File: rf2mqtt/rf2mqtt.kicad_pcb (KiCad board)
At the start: 2 copper layers, 64 x 56.5 mm, 25 parts, among them J1 Antenna Wire, Q1 TN0106N3-G, SW1 config, U1 Pico

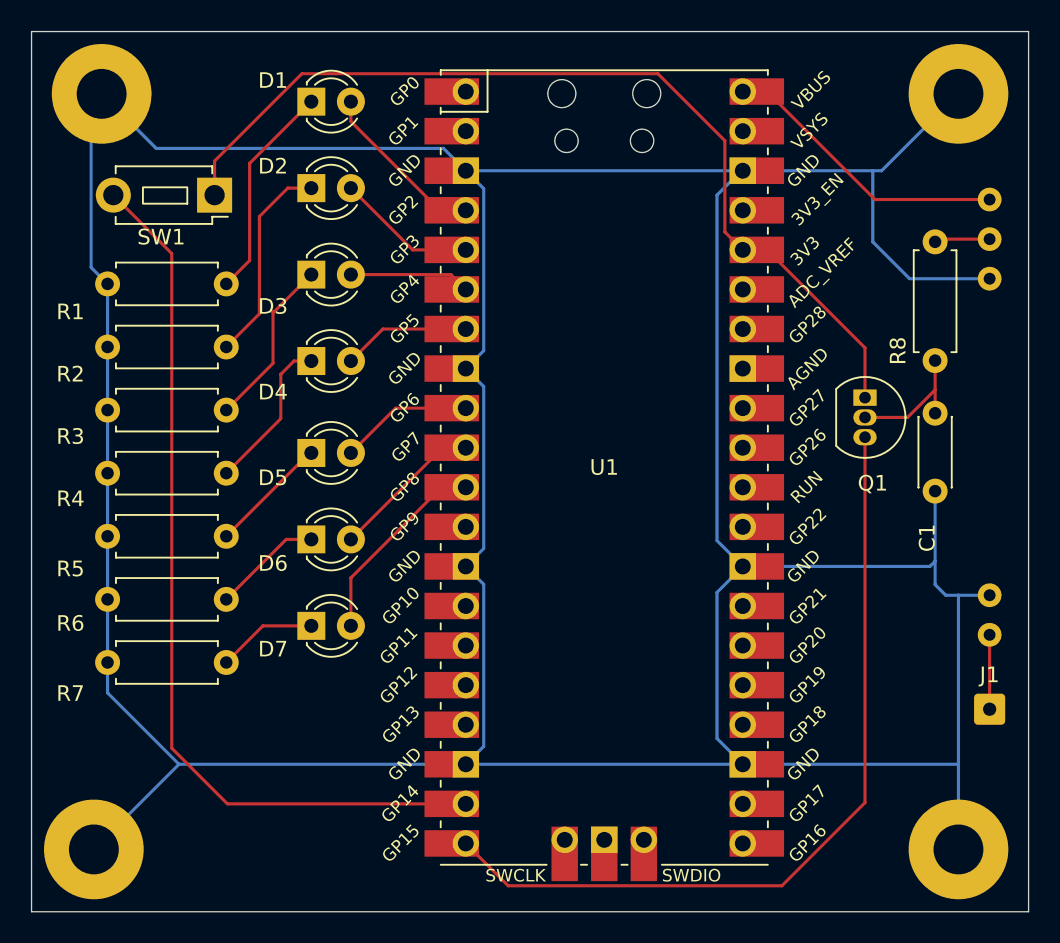
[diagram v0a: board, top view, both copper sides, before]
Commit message: Add debug MQTT messages
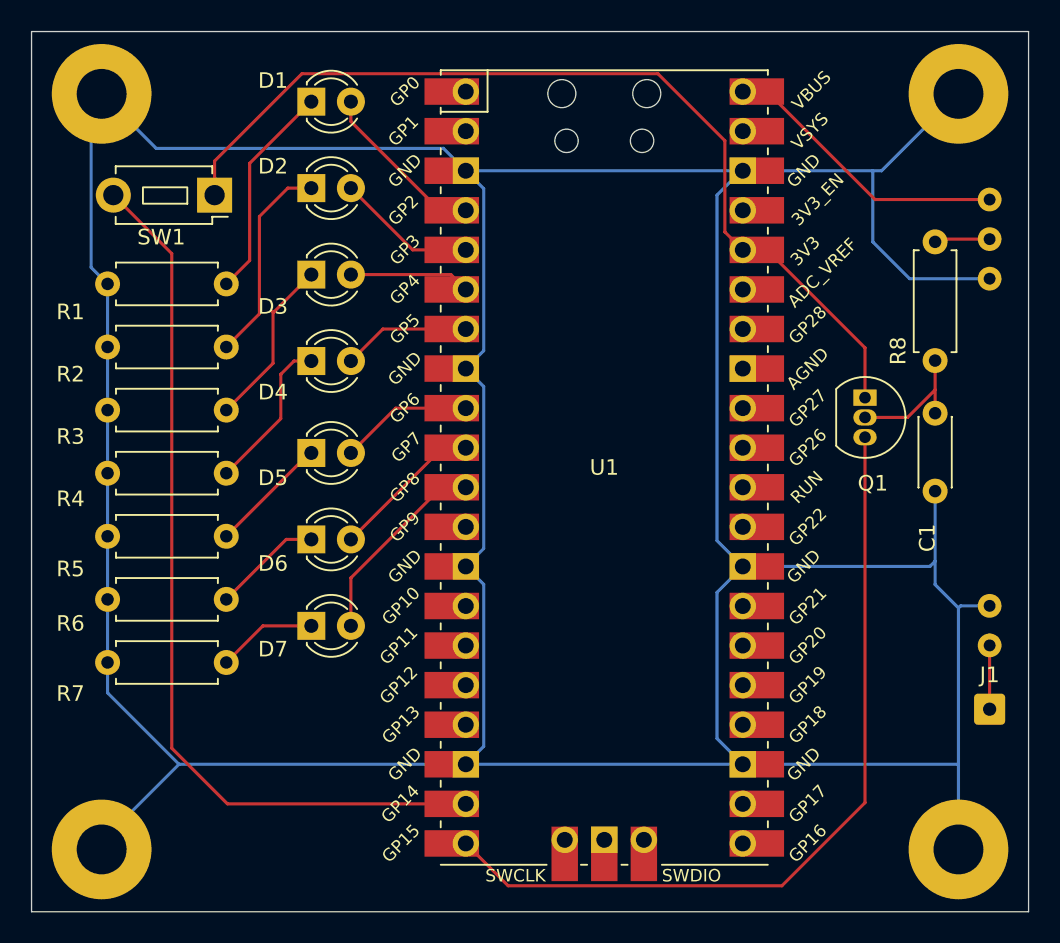
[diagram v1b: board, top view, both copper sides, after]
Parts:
- moved REF1 0.50 mm to (103.0, 110.0)
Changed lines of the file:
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@@
 		(grid_origin 105.98 118.54)
 		(pcbplotparams
-			(layerselection 0x00010fc_ffffffff)
+			(layerselection 0x00090ff_ffffffff)
 			(plot_on_all_layers_selection 0x0000000_00000000)
 			(disableapertmacros no)
@@
 			(outputformat 1)
 			(mirror no)
-			(drillshape 1)
+			(drillshape 0)
 			(scaleselection 1)
 			(outputdirectory "")
@@
 		(tags "Resistor Axial_DIN0207 series Axial Horizontal pin pitch 7.62mm 0.25W = 1/4W length 6.3mm diameter 2.5mm")
 		(property "Reference" "R8"
-			(at 0.62 -2.37 270)
+			(at 0.62 -2.37 -90)
 			(layer "F.SilkS")
 			(effects
@@
 		)
 		(property "Value" "10kΩ"
-			(at 6.62 -2.5 270)
+			(at 6.62 -2.5 -90)
 			(layer "F.Fab")
 			(effects
@@
 		)
 		(fp_text user "${REFERENCE}"
-			(at 3.81 0 270)
+			(at 3.81 0 -90)
 			(layer "F.Fab")
 			(effects
@@
 		(attr through_hole)
 		(fp_rect
-			(start -11.684 -1.016)
-			(end 19.812 2.032)
+			(start -12 -1.016)
+			(end 19 2.032)
 			(stroke
 				(width 0.05)
@@
 		)
 		(pad "4" thru_hole circle
-			(at -7.62 0.508 90)
+			(at -8.3 0.508 90)
 			(size 1.524 1.524)
 			(drill 0.762)
@@
 		)
 		(pad "5" thru_hole circle
-			(at -10.16 0.508 90)
+			(at -10.84 0.508 90)
 			(size 1.524 1.524)
 			(drill 0.762)
@@
 	(footprint "MountingHole:MountingHole_3.2mm_M3_Pad"
 		(layer "F.Cu")
-		(at 102.48 110.04)
+		(at 102.98 110.04)
 		(descr "Mounting Hole 3.2mm, M3")
 		(tags "mounting hole 3.2mm m3")
@@
 	)
 	(segment
-		(start 157.164 93.724)
-		(end 157.98 93.724)
+		(start 126.355 79.175)
+		(end 127.505 80.325)
 		(width 0.2)
 		(layer "B.Cu")
@@
 	)
 	(segment
-		(start 126.355 79.175)
-		(end 127.505 80.325)
+		(start 103.36 98.04)
+		(end 103.36 73.74)
 		(width 0.2)
 		(layer "B.Cu")
@@
 	)
 	(segment
-		(start 103.36 98.04)
-		(end 103.36 73.74)
+		(start 158.116 94.404)
+		(end 157.98 94.54)
 		(width 0.2)
 		(layer "B.Cu")
@@
 	)
 	(segment
-		(start 144.045 66.475)
-		(end 142.48 68.04)
+		(start 159.98 94.404)
+		(end 158.116 94.404)
 		(width 0.2)
 		(layer "B.Cu")
@@
 	)
 	(segment
-		(start 157.98 93.724)
-		(end 159.98 93.724)
+		(start 144.045 66.475)
+		(end 142.48 68.04)
 		(width 0.2)
 		(layer "B.Cu")
@@
 	)
 	(segment
-		(start 157.98 104.54)
-		(end 157.98 93.724)
+		(start 157.98 94.54)
+		(end 156.48 93.04)
 		(width 0.2)
 		(layer "B.Cu")
@@
 	)
 	(segment
-		(start 156.48 93.04)
-		(end 157.164 93.724)
+		(start 142.48 102.92)
+		(end 144.135 104.575)
 		(width 0.2)
 		(layer "B.Cu")
@@
 	)
 	(segment
-		(start 142.48 102.92)
-		(end 144.135 104.575)
+		(start 157.98 104.54)
+		(end 157.98 94.54)
 		(width 0.2)
 		(layer "B.Cu")

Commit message: Use hardware timers for LED blink to work around asyncio limitations and allow a nice long sleep cycle for the main loop.
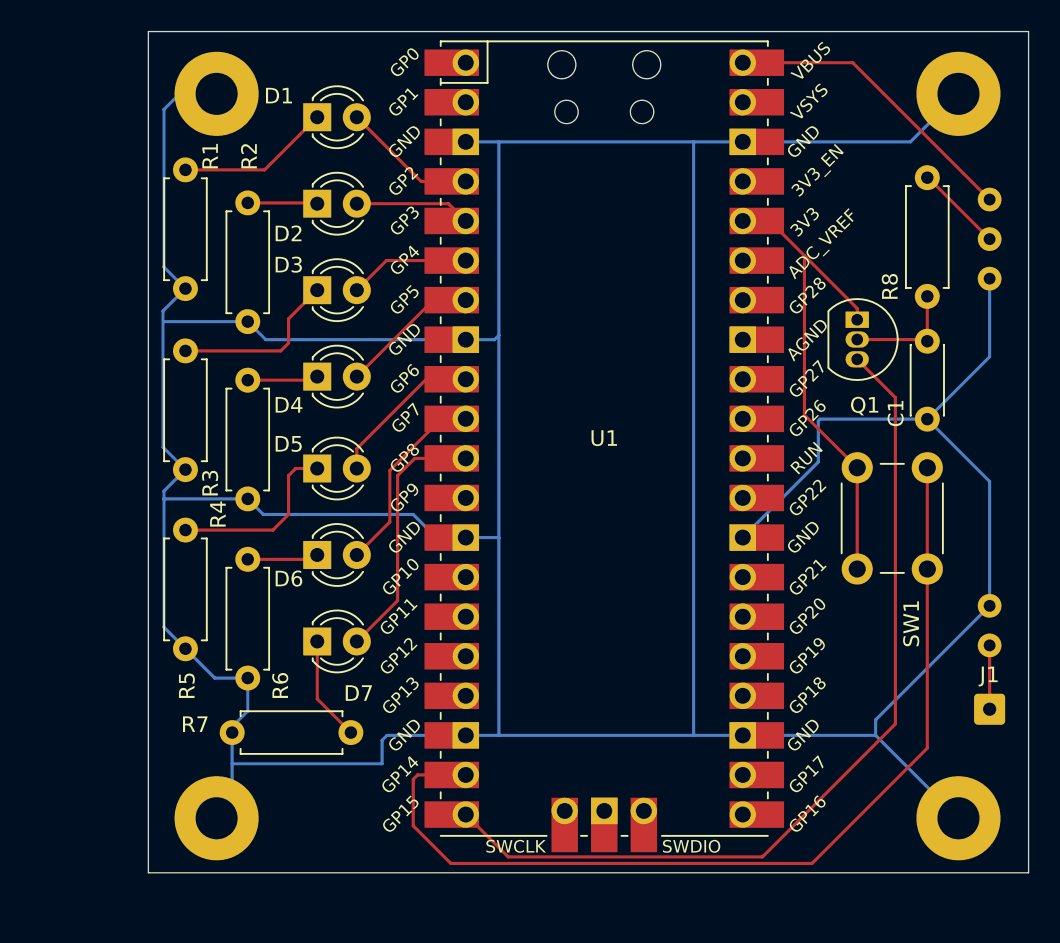
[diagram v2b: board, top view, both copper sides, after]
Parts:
- REF1 (x4): value MountingHole_3.2mm_M3_Pad -> MountingHole_2.7mm_M2.5_Pad; footprint MountingHole:MountingHole_3.2mm_M3_Pad -> MountingHole:MountingHole_2.7mm_M2.5_Pad
- SW1: footprint Button_Switch_THT:SW_PUSH_1P1T_6x3.5mm_H4.3_APEM_MJTP1243 -> Button_Switch_THT:SW_PUSH_6mm_H13mm
- moved SW1 47.7 mm to (151.5, 92.0), turned to 90 degrees
- moved R6 10.3 mm to (112.4, 99.0), turned to 90 degrees
- moved R7 9.18 mm to (111.4, 102.5)
- moved R4 9.15 mm to (112.4, 87.5), turned to 90 degrees
- moved R2 9.15 mm to (112.4, 76.2), turned to 90 degrees
- moved R5 8.78 mm to (108.4, 97.2), turned to 90 degrees
- moved REF1 7.65 mm to (110.4, 108.0)
- moved REF1 7.38 mm to (110.4, 61.5)
- moved R3 6.29 mm to (108.4, 85.7), turned to 90 degrees
- moved Q1 5.02 mm to (151.5, 76.0)
- moved R1 5.01 mm to (108.4, 74.0), turned to 90 degrees
- moved C1 4.65 mm to (156.0, 77.4)
- moved R8 4.15 mm to (156.0, 74.5)
- moved REF1 2.00 mm to (158.0, 108.0)
- moved U1 1.86 mm to (135.2, 83.7)
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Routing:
- net Net-(Q1-S): track 58.6 -> 30.2 mm
- net GND: track 294.5 -> 308.2 mm
- net Net-(D2-K): track 13.3 -> 4.41 mm
- net Net-(D4-K): track 10.1 -> 4.23 mm
- net Net-(D7-A): track 11.3 -> 16.6 mm
- net Net-(Q1-D): track 52.4 -> 56.7 mm
- net Net-(U1-GPIO14): track 57.4 -> 61.5 mm
- net Net-(D1-K): track 14.0 -> 9.86 mm
- net Net-(D5-K): track 7.57 -> 11.6 mm
- net Net-(D6-K): track 7.05 -> 4.18 mm
- net Net-(D6-A): track 8.32 -> 11.0 mm
- net +5V: track 17.2 -> 19.5 mm
- net Net-(RF1-DATA): track 3.32 -> 5.58 mm
- net Net-(Q1-G): track 8.61 -> 6.89 mm
- net Net-(D2-A): track 9.02 -> 7.45 mm
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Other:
- board size 64 x 56.5 mm -> 56.5 x 54 mm
